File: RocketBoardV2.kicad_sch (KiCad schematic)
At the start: 6 parts, among them U1 SC0914_13_, U2 MT29F2G01ABAGDWB-IT-G, U3 BMI270

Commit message: started routing
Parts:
- added C1, C2, C3: C, symbol Device:C
- added C4, C5, C6: 0.1uF, symbol Device:C
- added C7, C8: 15pF, symbol Device:C
- added J1: 10118194-0001LF, Components:AMPHENOL_10118194-0001LF, symbol 10118194-0001LF:10118194-0001LF
- added R3: 1K, symbol Device:R
- added Y1: ABM8-272-T3, Components:XTAL_ABM8-272-T3, symbol ABM8-272-T3:ABM8-272-T3
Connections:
- net SPI0_RX: now reaches U3.1 (SDO)
- net SPI0_RX: now also A1.7 (INT/SDO), U1.2 (GPIO0)
- net GYRO_CS: now reaches U3.12 (CSB)
- net GYRO_CS: now also U1.3 (GPIO1)
- net SPI0_SCK: now reaches U3.13 (SCX)
- net SPI0_SCK: now also A1.2 (SCL/SCLK), U1.4 (GPIO2)
- net SPI0_TX: now reaches U3.14 (SDX)
- net SPI0_TX: now also A1.4 (SDA/SDI), U1.5 (GPIO3)
- net +1V8: now reaches U3.5 (VDDIO)
- net +1V8: now also A1.10 (VDD), U3.8 (VDD), C4.1, C5.1, C6.1
- net GND: now reaches U3.6 (GNDIO)
- net GND: now also A1.3 (GND), A1.8 (GND__1), A1.9 (GND__2), U1.19 (TESTEN), U1.57 (GND), U2.4 (VSS), U3.7 (GND), C1.2, C2.2, C3.2, C4.2, C5.2, C6.2, C7.2, C8.2, J1.5 (GND), J1.SH1 (SHIELD), J1.SH2 (SHIELD__1), J1.SH3 (SHIELD__2), J1.SH4 (SHIELD__3), J1.SH5 (SHIELD__4), J1.SH6 (SHIELD__5), Y1.2 (GND), Y1.4 (GND__1)
- net USB_D-: now reaches R1.2
- net USB_D-: now also J1.2 (D-)
- net QSPI_SS: now reaches U2.1 (~{CS})
- net QSPI_SS: now also U1.56 (QSPI_SS_N)
- net QSPI_SD1: now reaches U2.2 (SO/IO1)
- net QSPI_SD1: now also U1.55 (QSPI_SD1)
- net QSPI_SD2: now reaches U2.3 (~{WP}/IO2)
- net QSPI_SD2: now also U1.54 (QSPI_SD2)
- net QSPI_SD0: now reaches U2.5 (SI/IO0)
- net QSPI_SD0: now also U1.53 (QSPI_SD0)
- net QSPI_SCLK: now reaches U2.6 (SCK)
- net QSPI_SCLK: now also U1.52 (QSPI_SCLK)
- net QSPI_SD3: now reaches U2.7 (~{HOLD}/IO3)
- net QSPI_SD3: now also U1.51 (QSPI_SD3)
- net XIN: now reaches U1.20 (XIN)
- net XIN: now also C7.1, Y1.1
- net XOUT: now reaches U1.21 (XOUT)
- net XOUT: now also R3.1
- net +1V1: now reaches U1.23 (DVDD)
- net +1V1: now also U1.45 (VREG_VOUT), U1.50 (DVDD__1), C1.1, C2.1, C3.1
- net BARO_CS: now reaches U1.6 (GPIO4)
- net BARO_CS: now also A1.6 (~{CS})
- net USB_D+: now reaches R2.2
- net USB_D+: now also J1.3 (D+)
- new net: C8.1, R3.2, Y1.3
- new net VBUS: J1.1 (VCC)
- no-connect marks 0 -> 5
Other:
- moved on the sheet: A1, R1, R2, U1, U2, U3

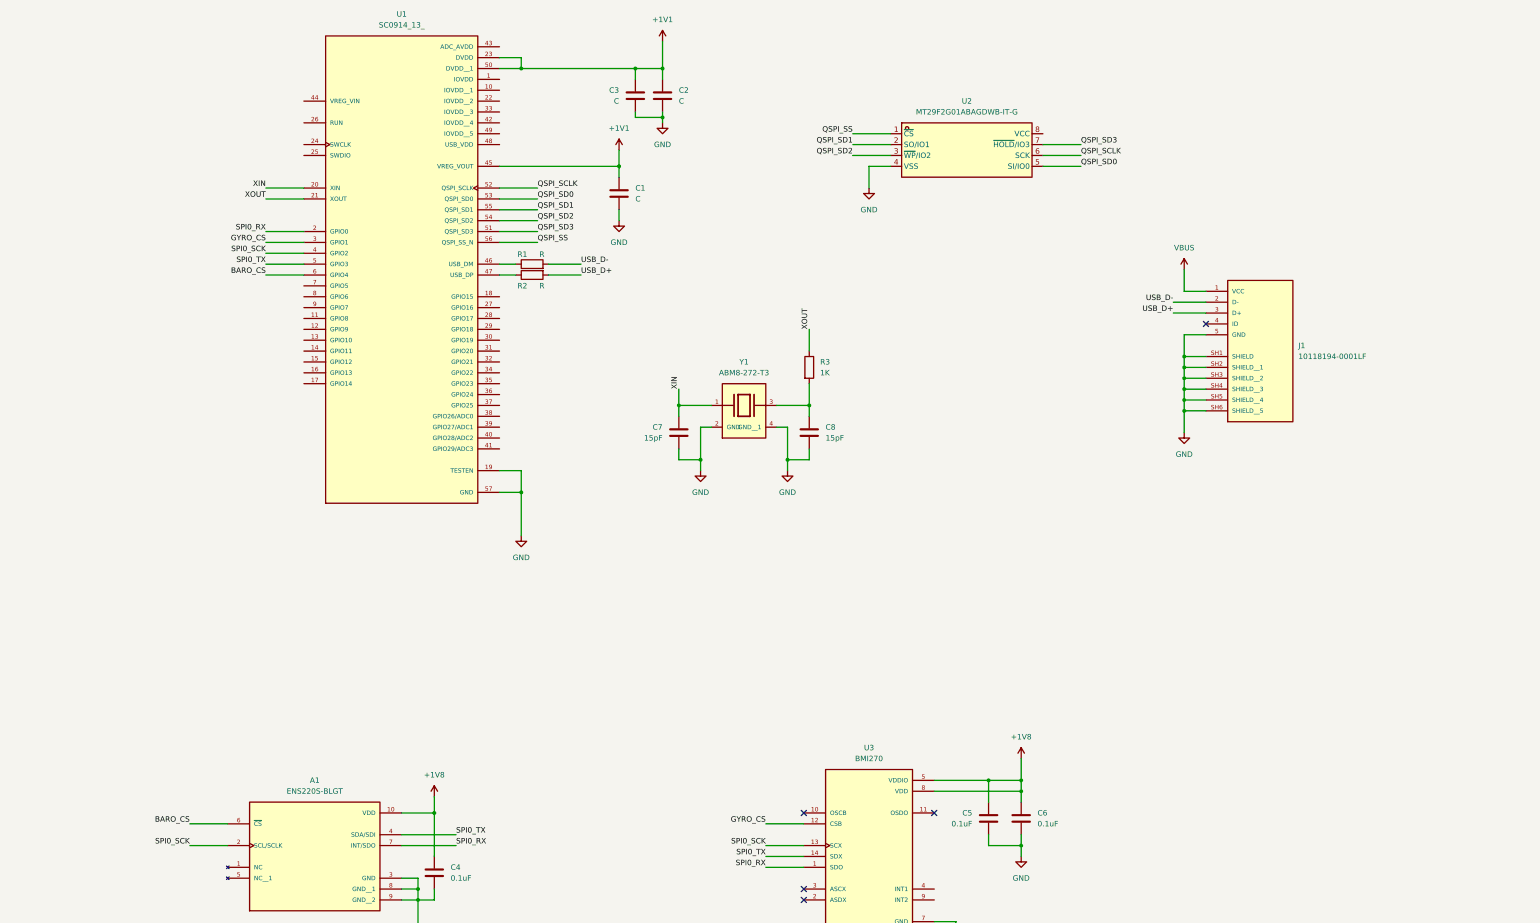
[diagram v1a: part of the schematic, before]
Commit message: added PMIC
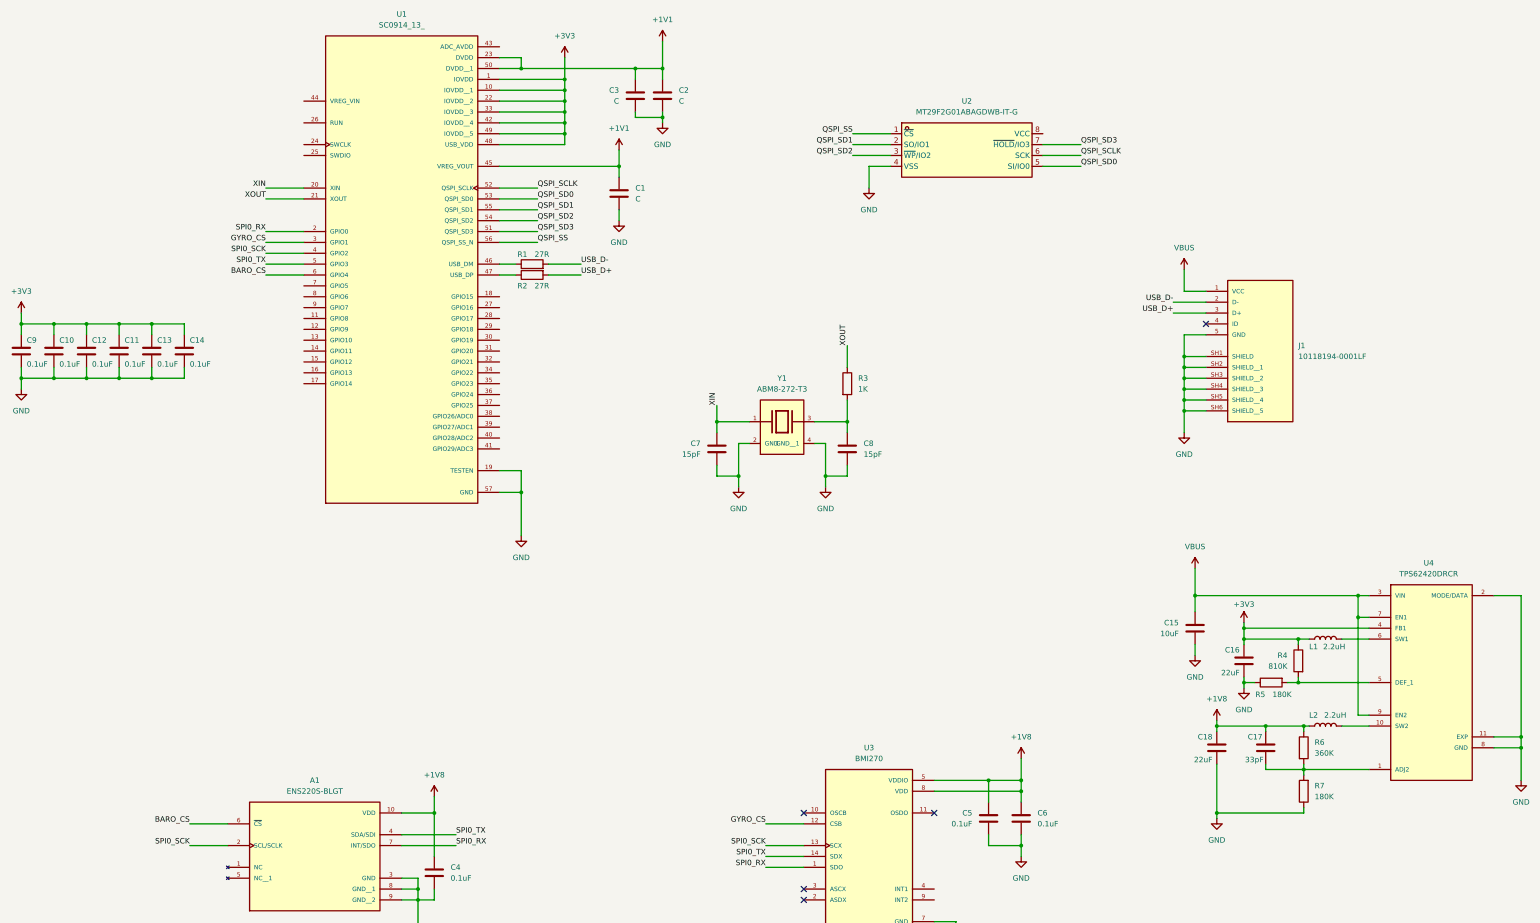
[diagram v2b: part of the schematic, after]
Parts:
- added C10, C11, C12, C13, C14, C9: 0.1uF, symbol Device:C
- added C15: 10uF, symbol Device:C
- added C16, C18: 22uF, symbol Device:C
- added C17: 33pF, symbol Device:C
- added L1, L2: 2.2uH, symbol Device:L
- added R4: 810K, symbol Device:R
- added R5, R7: 180K, symbol Device:R
- added R6: 360K, symbol Device:R
- added U4: TPS62420DRCR, TPS62420DRCR:IC_TPS62420DRCR, symbol TPS62420DRCR:TPS62420DRCR
- R1, R2: value R -> 27R
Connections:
- net +1V8: now also C17.1, C18.1, L2.1, R6.1
- net GND: now also C10.2, C11.2, C12.2, C13.2, C14.2, C15.2, C16.2, C18.2, C9.2, R5.1, R7.1, U4.11 (EXP), U4.2 (MODE/DATA), U4.8 (GND)
- net VBUS: now also C15.1, U4.3 (VIN), U4.7 (EN1), U4.9 (EN2)
- net +3V3: now reaches U1.1 (IOVDD)
- net +3V3: now also U1.10 (IOVDD__1), U1.22 (IOVDD__2), U1.33 (IOVDD__3), U1.42 (IOVDD__4), U1.48 (USB_VDD), U1.49 (IOVDD__5), C10.1, C11.1, C12.1, C13.1, C14.1, C16.1, C9.1, L1.1, R4.1, U4.4 (FB1)
- new net: L2.2, U4.10 (SW2)
- new net: C17.2, R6.2, R7.2, U4.1 (ADJ2)
- new net: R4.2, R5.2, U4.5 (DEF_1)
- new net: L1.2, U4.6 (SW1)
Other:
- moved on the sheet: C7, C8, R3, Y1

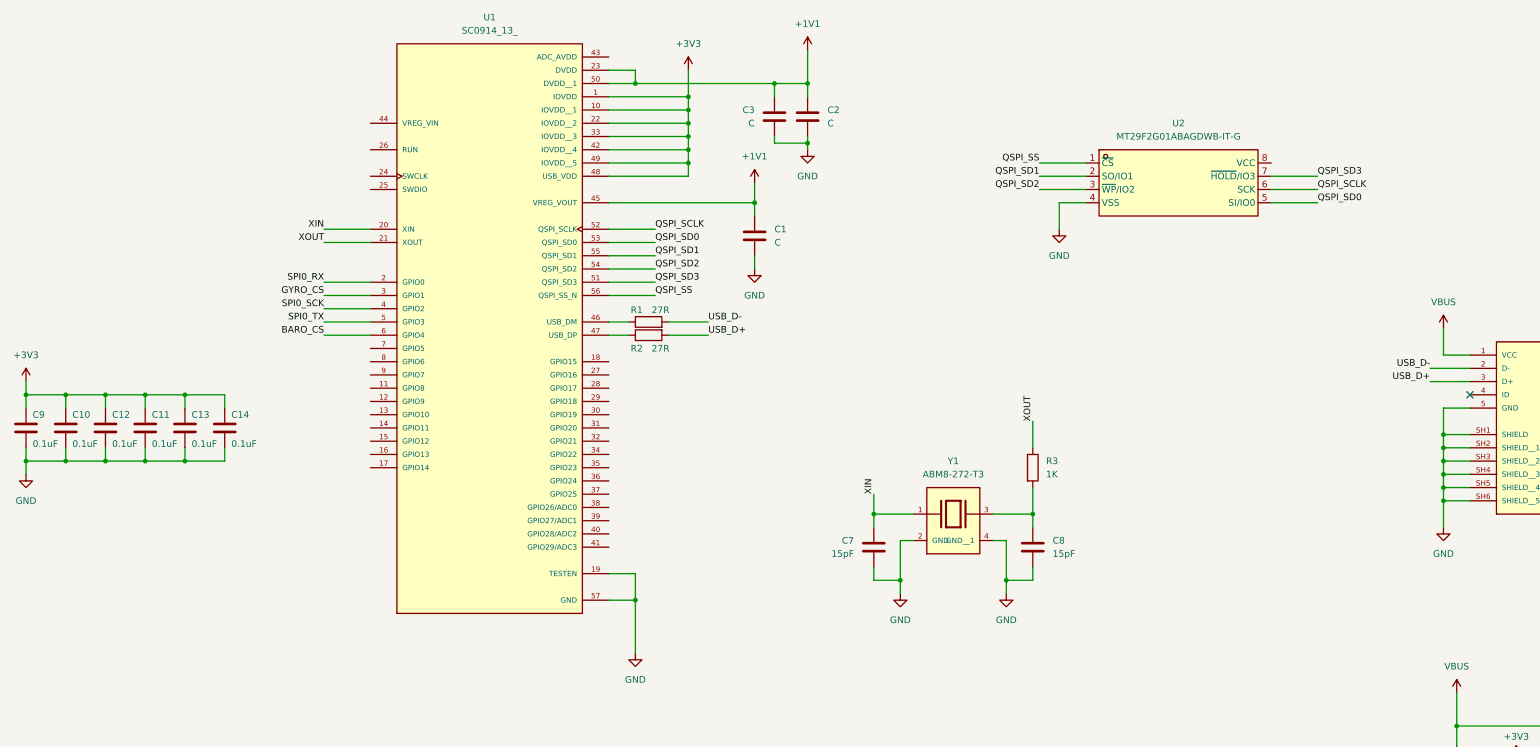
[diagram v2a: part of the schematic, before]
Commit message: some more power changes
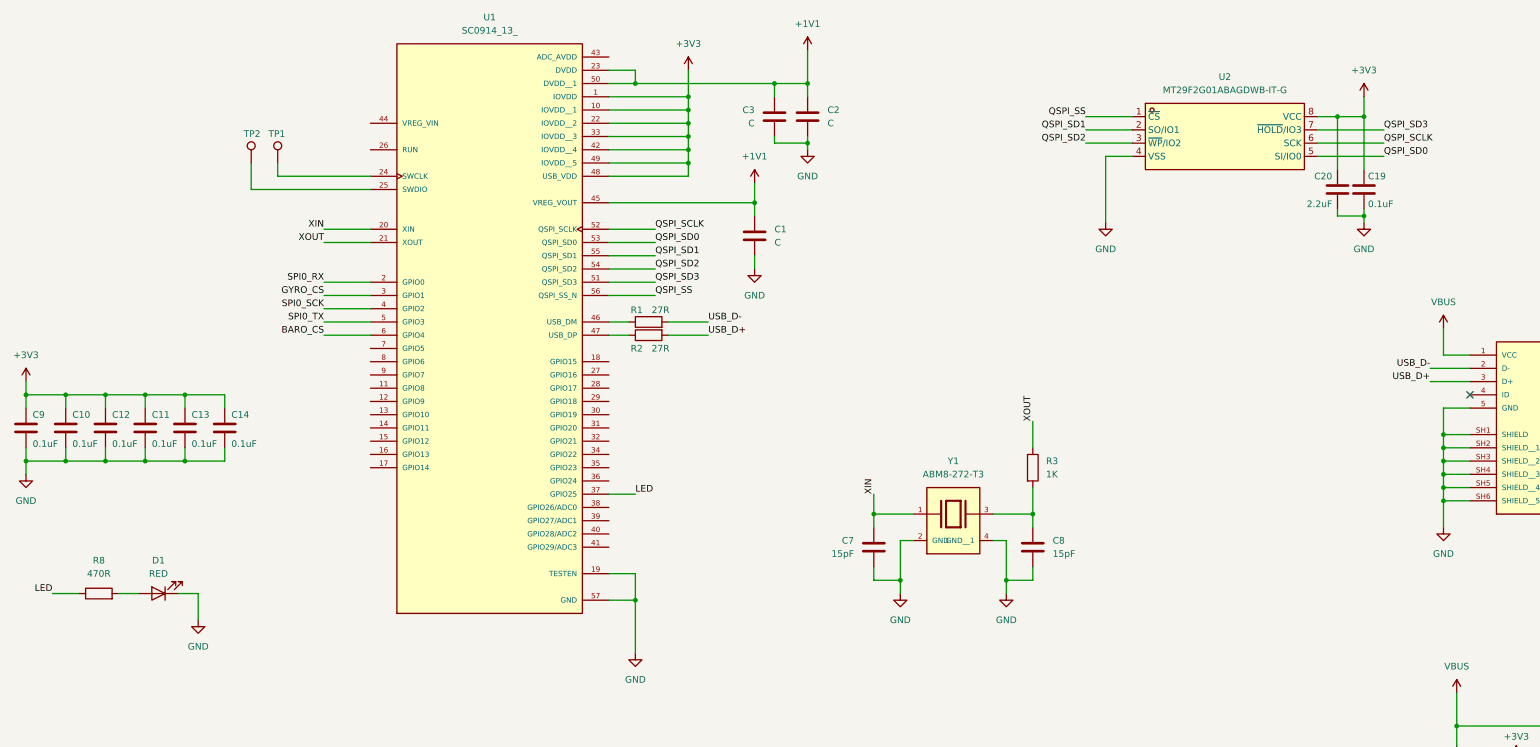
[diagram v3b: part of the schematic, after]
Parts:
- added C19: 0.1uF, symbol Device:C
- added C20: 2.2uF, symbol Device:C
- added D1: RED, symbol Device:LED
- added R8: 470R, symbol Device:R
- added TP1, TP2: TestPoint, symbol Connector:TestPoint
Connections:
- net +3V3: now also U2.8 (VCC), C19.1, C20.1
- net GND: now also C19.2, C20.2, D1.1 (K)
- net at U1.24 (SWCLK): now also TP1.1
- net at U1.25 (SWDIO): now also TP2.1
- net LED: now reaches U1.37 (GPIO25)
- net LED: now also R8.1
- new net: D1.2 (A), R8.2
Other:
- moved on the sheet: U2

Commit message: changed flash, power changes
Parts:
- removed U2: MT29F2G01ABAGDWB-IT-G, easyeda2kicad:U-PDFN-8_L6.0-W8.0-P1.27-BL, symbol easyeda2kicad:MT29F2G01ABAGDWB-IT-G
- added C21, C22: 1uF, symbol Device:C
- added C23: 2.2uF, symbol Device:C
- added C24, C25: 0.1uF, symbol Device:C
- added C26: 0.33uF, symbol Device:C
- added D2: RED, symbol Device:LED
- added D3, D4: D, symbol Device:D
- added IC1: W25Q256JVEIQ, Components:SON127P800X600X80-9N, symbol W25Q256JVEIQ:W25Q256JVEIQ
- added J3: Conn_01x03_Pin, Connector_PinHeader_2.54mm:PinHeader_1x03_P2.54mm_Horizontal, symbol Connector:Conn_01x03_Pin
- added R10: 1K, symbol Device:R
- added R11, R12: 10K, symbol Device:R
- added R13, R9: 470R, symbol Device:R
- added S1, S2: TL3315NF250Q, Components:SW_TL3315NF250Q, symbol TL3315NF250Q:TL3315NF250Q
- added TP3, TP4: TestPoint, TestPoint:TestPoint_Pad_3.0x3.0mm, symbol Connector:TestPoint
- added U2: W25Q16JVUXIQ_TR, Components:IC_W25Q16JVUXIQ_TR, symbol W25Q16JVUXIQ_TR:W25Q16JVUXIQ_TR
- added VR1: UA78L05ACPK, Components:VREG_UA78L05ACPK, symbol UA78L05ACPK:UA78L05ACPK
- C1, C2, C3: value C -> 1uF
- D1: value RED -> GREEN
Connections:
- net +3V3: now also U1.43 (ADC_AVDD), U1.44 (VREG_VIN), C22.1, C23.1, C24.1, IC1.3 (DO_(IO1)_2), IC1.7 (IO3), IC1.8 (VCC), R11.1, R12.1, R13.1, R9.2, U2.8 (VCC)
- net GND: now also C21.2, C22.2, C23.2, C24.2, C25.2, C26.2, D2.1 (K), IC1.4 (GND), IC1.9 (EP), J3.3 (Pin_3), S1.3, S1.4, S2.1, S2.2, TP4.1, U2.4 (GND), U2.9 (EXP), VR1.2 (COMMON)
- net QSPI_SCLK: now also U2.6 (CLK)
- net QSPI_SD0: now also U2.5 (DI/IO0)
- net QSPI_SD1: now also U2.2 (DO/IO1)
- net QSPI_SD2: now also U2.3 (~{WP}/IO2)
- net QSPI_SD3: now also U2.7 (~{HOLD}/~{RESET}/IO3)
- net QSPI_SS: now also R10.2, R11.2, U2.1 (~{CS})
- net SPI1_SCK: now reaches U1.13 (GPIO10)
- net SPI1_SCK: now also IC1.6 (CLK)
- net SPI1_TX: now reaches U1.14 (GPIO11)
- net SPI1_TX: now also IC1.5 (DI_(IO0))
- net SPI1_RX: now reaches U1.15 (GPIO12)
- net SPI1_RX: now also IC1.2 (DO_(IO1)_1)
- net FLASH_CS: now reaches U1.16 (GPIO13)
- net FLASH_CS: now also IC1.1 (/CS), R12.2
- net RUN: now reaches U1.26 (RUN)
- net RUN: now also C21.1, R9.1, S1.1, S1.2
- net SERVO: now reaches U1.7 (GPIO5)
- net SERVO: now also J3.1 (Pin_1)
- net VBUS renamed +5V
- net +5V: now also D3.1 (K), D4.1 (K), J3.2 (Pin_2); no longer J1.1 (VCC)
- new net: C25.1, D3.2 (A), VR1.1 (OUTPUT)
- new net: R10.1, S2.3, S2.4
- new net: D2.2 (A), R13.2
- new net: D4.2 (A), J1.1 (VCC)
- new net +BATT: C26.1, TP3.1, VR1.3 (INPUT)
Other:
- moved on the sheet: A1, C10, C11, C12, C13, C14, C15, C16, C17, C18, C19, C20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

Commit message: organized schematic
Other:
- note added: "5V LDO"
- note added: "Barometer"
- note added: "Battery Contacts"
- note added: "Crystal"
- note added: "Decaps"
- note added: "Flight Log Flash"
- note added: "Gyro/Accelerometer"
- note added: "PMIC"
- note added: "Program Flash"
- note added: "Reset Button"
- note added: "Servo Pins"
- note added: "Status LEDs"
- note added: "USB"
- moved on the sheet: A1, C1, C10, C11, C12, C13, C14, C15, C16, C17, C18, C19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

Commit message: basic layout
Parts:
- added H1, H2, H3, H4: MountingHole, MountingHole:MountingHole_3mm, symbol Mechanical:MountingHole
- added R14, R15: 10K, symbol Device:R
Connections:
- net +3V3: now also R14.1, R15.1; no longer IC1.3 (DO_(IO1)_2), IC1.7 (IO3)
- new net: IC1.3 (DO_(IO1)_2), R14.2
- new net: IC1.7 (IO3), R15.2
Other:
- note added: "Mounting Holes"
- moved on the sheet: C1, C10, C11, C12, C13, C14, C2, C22, C3, C7, C8, C9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
